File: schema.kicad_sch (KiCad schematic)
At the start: 5 parts, among them U1 74HC595D, U2 74HC595D, U5 AT28C256-15PU

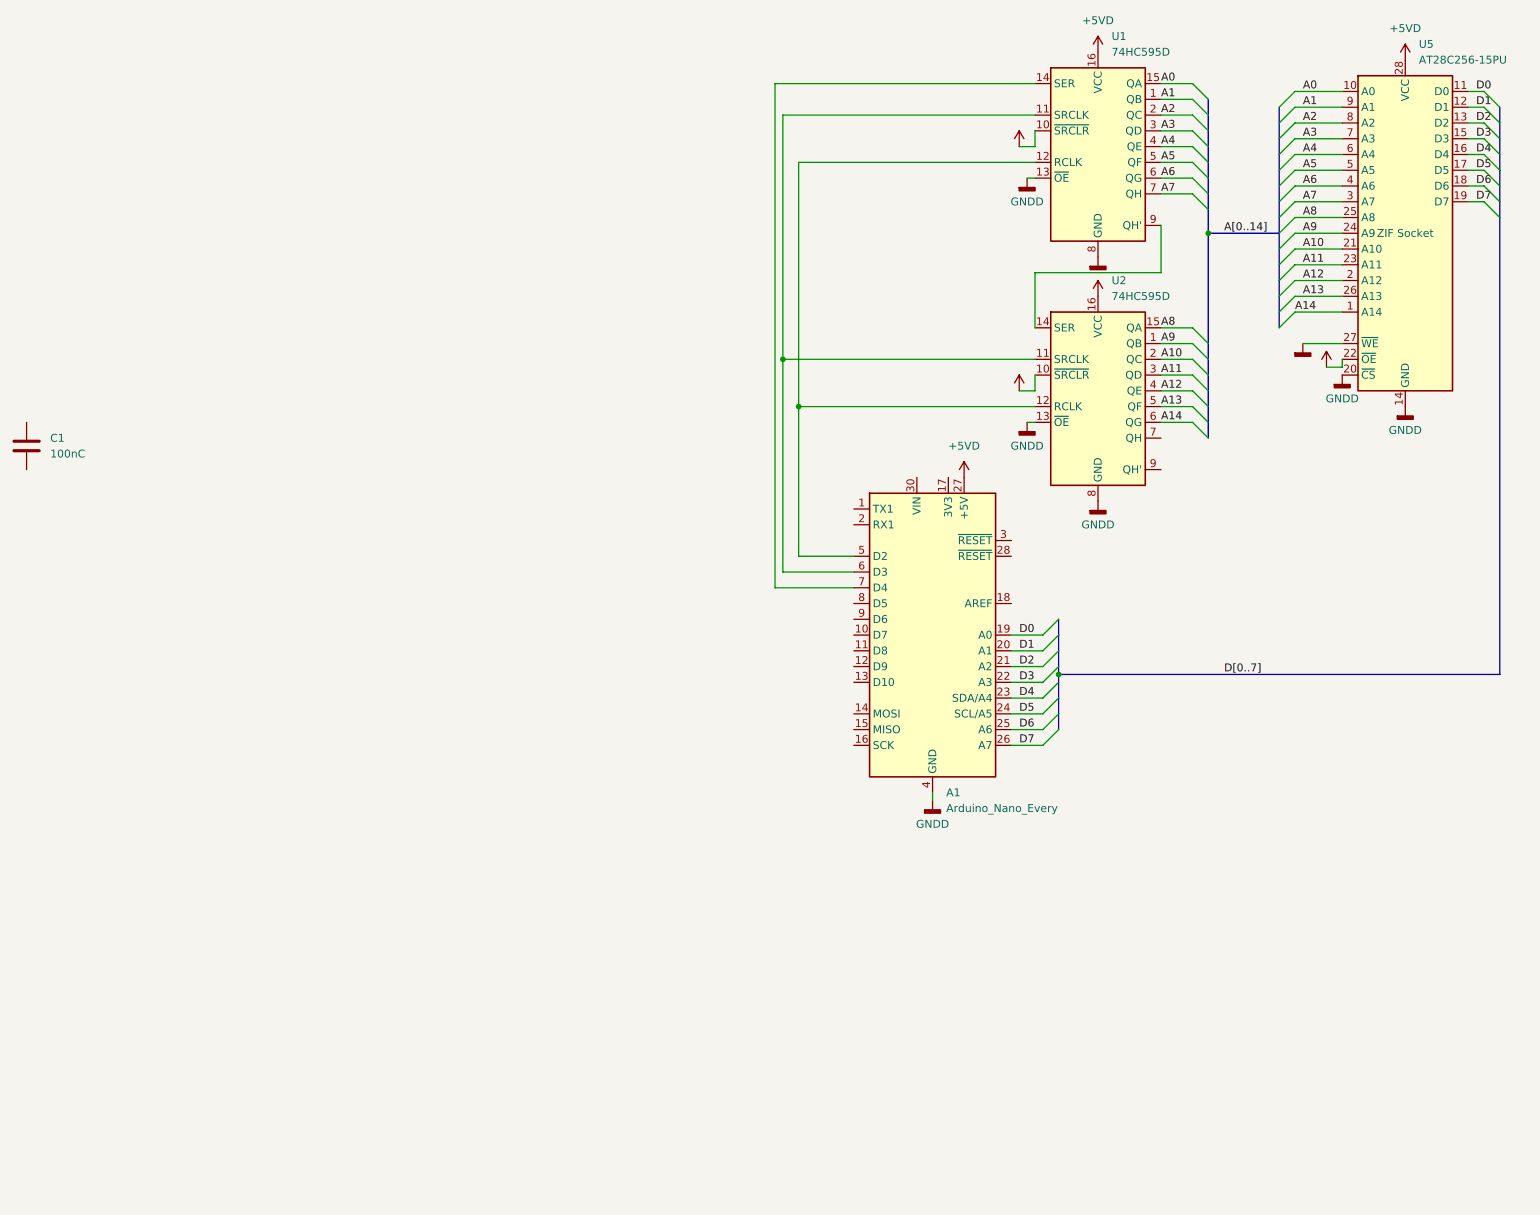
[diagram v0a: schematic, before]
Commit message: Add condensators how I think is right
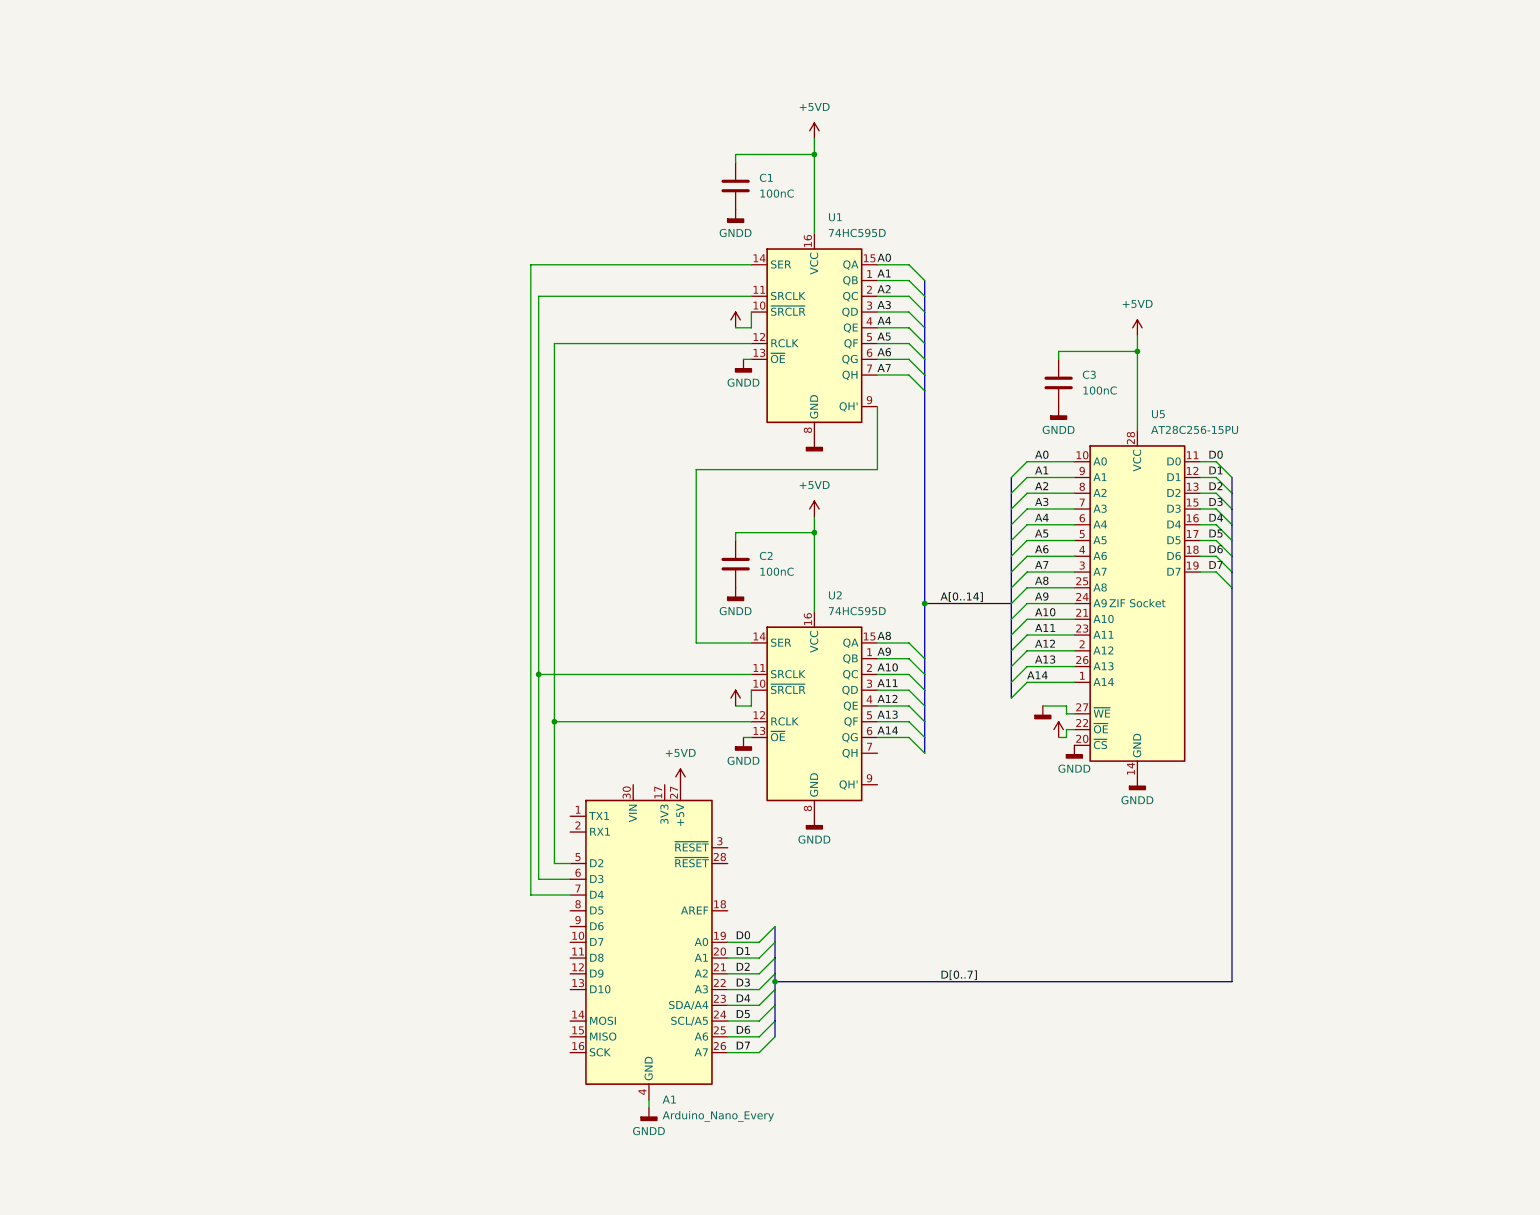
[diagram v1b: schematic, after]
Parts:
- added C2, C3: 100nC, Capacitor_SMD:C_0805_2012Metric_Pad1.18x1.45mm_HandSolder, symbol Device:C
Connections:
- net +5VD: now also C1.1, C2.1, C3.1
- net GNDD: now also C1.2, C2.2, C3.2
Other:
- moved on the sheet: A1, C1, U1, U2, U5

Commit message: Connect Control pins to MCU in schema
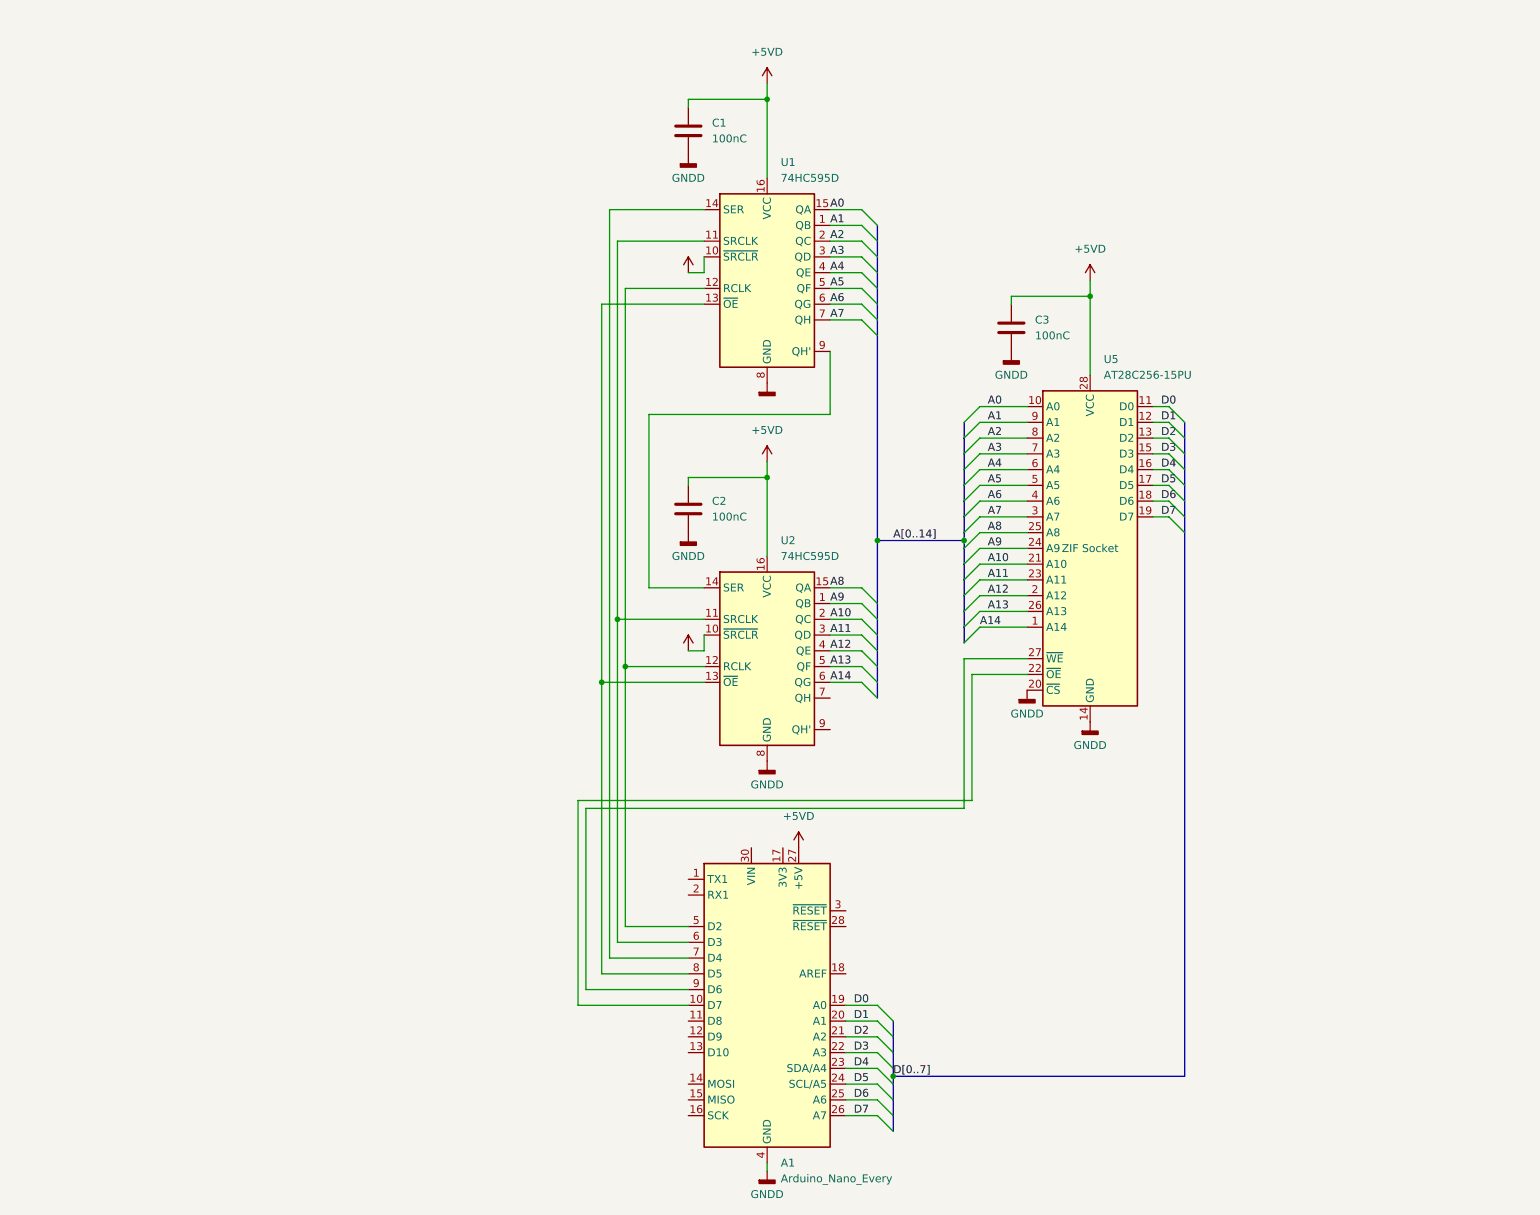
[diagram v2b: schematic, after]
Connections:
- net +5VD: no longer U5.22 (~{OE})
- net GNDD: no longer U1.13 (~{OE}), U2.13 (~{OE}), U5.27 (~{WE})
- net at A1.10 (D7): now also U5.22 (~{OE})
- net at A1.8 (D5): now also U1.13 (~{OE}), U2.13 (~{OE})
- net at A1.9 (D6): now also U5.27 (~{WE})
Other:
- moved on the sheet: A1, C1, C2, C3, U1, U2, U5
